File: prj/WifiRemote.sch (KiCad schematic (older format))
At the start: 68 parts, among them J1 DIP-BLACK-MALE-HEADER-VERT_4P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, J2 DIP-BLACK-MALE-HEADER_6P-2.54_, K1 DIP-SWITCH-TACTILE-SPST-NO_TS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, K2 DIP-SWITCH-TACTILE-SPST-NO_TS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, K3 DIP-SWITCH-TACTILE-SPST-NO_TS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, K4 DIP-SWITCH-TACTILE-SPST-NO_TS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, M1 Mechanical_Mount, M2 Mechanical_Mount, M3 Mechanical_Mount, M4 Mechanical_Mount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

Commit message: Changed button GPIO association and updated mechanical mount pin
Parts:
- M1, M2, M3, M4: footprint ICEE-Mechanical:mounting_panhead6_5mm -> (none)
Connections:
- net GPIO12: now also C9.2, D14.1, R30.1; no longer C6.2, D10.1, R27.1
- net GPIO13: now also D11.A (+), D7.A (+), D8.A (+), D9.A (+), R26.2; no longer C8.2, D13.1, R29.1
- net GPIO14: now also C8.2, D13.1, R29.1; no longer C9.2, D14.1, R30.1
- net GPIO4: now also C6.2, D10.1, R27.1; no longer D11.A (+), D7.A (+), D8.A (+), D9.A (+), R26.2
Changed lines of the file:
@@
 Text GLabel 6700 1400 2    39   Input ~ 0
 ESP_ADC
-Text GLabel 5675 3975 2    39   Input ~ 0
+Text GLabel 1325 3975 0    39   Input ~ 0
 GPIO4
 Text GLabel 2075 4225 0    39   Input ~ 0
 GPIO5
-Text GLabel 1325 3975 0    39   Input ~ 0
+Text GLabel 3750 4725 0    39   Input ~ 0
 GPIO12
+Text GLabel 5675 3975 2    39   Input ~ 0
+GPIO13
 Text GLabel 2950 4475 0    39   Input ~ 0
-GPIO13
-Text GLabel 3750 4725 0    39   Input ~ 0
 GPIO14
 $Comp
@@
 	4675 3975 1775 3975
 $Comp
-L Mechanical_Mount M1
-U 1 1 59BB9484
-P 7250 5800
-F 0 "M1" H 7150 5875 45  0000 L BNN
-F 1 "Mechanical_Mount" H 7050 5600 45  0001 L BNN
-F 2 "ICEE-Mechanical:mounting_panhead6_5mm" H 7250 5800 60  0001 C CNN
-F 3 "" H 7250 5800 60  0001 C CNN
-	1    7250 5800
-	1    0    0    -1
-$EndComp
-$Comp
-L Mechanical_Mount M2
-U 1 1 59BB9AA5
-P 7475 5800
-F 0 "M2" H 7375 5875 45  0000 L BNN
-F 1 "Mechanical_Mount" H 7275 5600 45  0001 L BNN
-F 2 "ICEE-Mechanical:mounting_panhead6_5mm" H 7475 5800 60  0001 C CNN
-F 3 "" H 7475 5800 60  0001 C CNN
-	1    7475 5800
-	1    0    0    -1
-$EndComp
-$Comp
-L Mechanical_Mount M3
-U 1 1 59BB9B95
-P 7700 5800
-F 0 "M3" H 7600 5875 45  0000 L BNN
-F 1 "Mechanical_Mount" H 7500 5600 45  0001 L BNN
-F 2 "ICEE-Mechanical:mounting_panhead6_5mm" H 7700 5800 60  0001 C CNN
-F 3 "" H 7700 5800 60  0001 C CNN
-	1    7700 5800
-	1    0    0    -1
-$EndComp
-$Comp
 L GNDD #PWR037
 U 1 1 59BC0554
@@
 F 3 "" H 7925 5900 50  0000 C CNN
 	1    7925 5900
-	1    0    0    -1
-$EndComp
-$Comp
-L Mechanical_Mount M4
-U 1 1 59BBA5DF
-P 7925 5800
-F 0 "M4" H 7825 5875 45  0000 L BNN
-F 1 "Mechanical_Mount" H 7725 5600 45  0001 L BNN
-F 2 "ICEE-Mechanical:mounting_panhead6_5mm" H 7925 5800 60  0001 C CNN
-F 3 "" H 7925 5800 60  0001 C CNN
-	1    7925 5800
 	1    0    0    -1
 $EndComp
@@
 	0    1    1    0
 $EndComp
+$Comp
+L Mechanical_Mount M1
+U 1 1 59C34B45
+P 7250 5800
+F 0 "M1" H 7150 5875 45  0000 L BNN
+F 1 "Mechanical_Mount" H 7300 5700 45  0001 L BNN
+F 2 "" H 7250 5800 60  0001 C CNN
+F 3 "" H 7250 5800 60  0001 C CNN
+	1    7250 5800
+	1    0    0    -1
+$EndComp
+$Comp
+L Mechanical_Mount M2
+U 1 1 59C35BEC
+P 7475 5800
+F 0 "M2" H 7375 5875 45  0000 L BNN
+F 1 "Mechanical_Mount" H 7525 5700 45  0001 L BNN
+F 2 "" H 7475 5800 60  0001 C CNN
+F 3 "" H 7475 5800 60  0001 C CNN
+	1    7475 5800
+	1    0    0    -1
+$EndComp
+$Comp
+L Mechanical_Mount M3
+U 1 1 59C35CD4
+P 7700 5800
+F 0 "M3" H 7600 5875 45  0000 L BNN
+F 1 "Mechanical_Mount" H 7750 5700 45  0001 L BNN
+F 2 "" H 7700 5800 60  0001 C CNN
+F 3 "" H 7700 5800 60  0001 C CNN
+	1    7700 5800
+	1    0    0    -1
+$EndComp
+$Comp
+L Mechanical_Mount M4
+U 1 1 59C35DC5
+P 7925 5800
+F 0 "M4" H 7825 5875 45  0000 L BNN
+F 1 "Mechanical_Mount" H 7975 5700 45  0001 L BNN
+F 2 "" H 7925 5800 60  0001 C CNN
+F 3 "" H 7925 5800 60  0001 C CNN
+	1    7925 5800
+	1    0    0    -1
+$EndComp
 $EndSCHEMATC

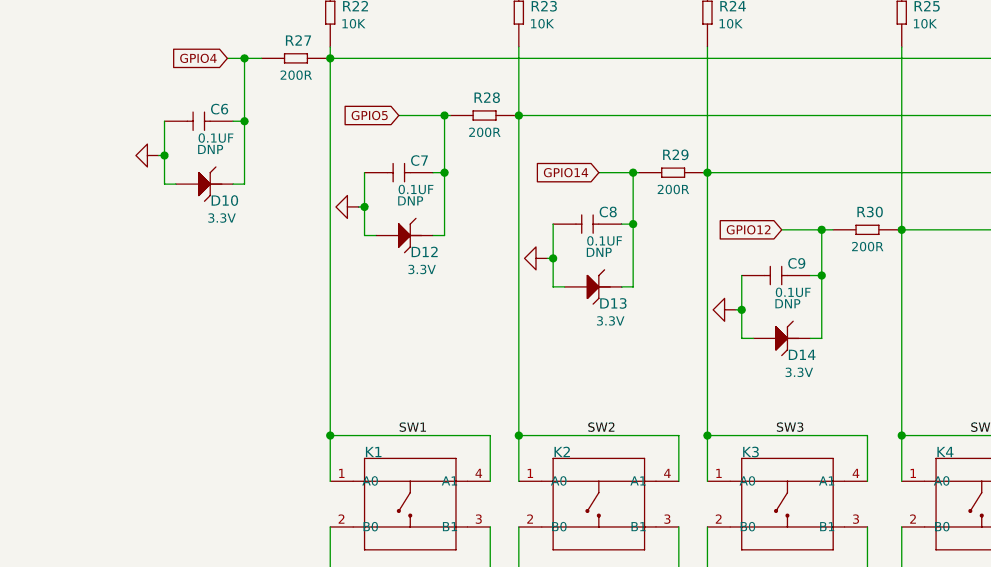
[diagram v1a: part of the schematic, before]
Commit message: Updated TVS diode pinout
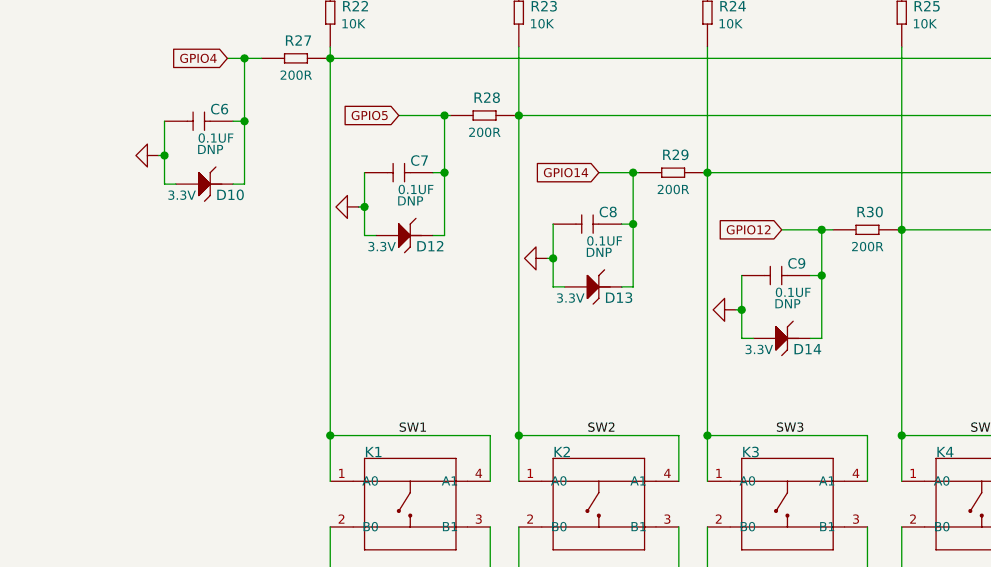
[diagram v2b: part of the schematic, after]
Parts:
- D10, D12, D13, D14, D4: footprint Diodes_SMD:SOD-523 -> Diodes_SMD:D_SOD-523
- M1, M2, M3, M4: footprint (none) -> ICEE-Mechanical:mounting_panhead6_5mm
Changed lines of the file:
@@
 NoConn ~ 250  -550
-$Comp
-L SMD-Diode-TVS-3.3VMW-15V-SOD-523 D14
-U 1 1 59B6E445
-P 3775 5200
-F 0 "D14" H 3775 5100 45  0000 L BNN
-F 1 "SMD-Diode-TVS-3.3VMW-15V-SOD-523" H 3625 5050 45  0001 L BNN
-F 2 "Diodes_SMD:SOD-523" H 3775 5200 60  0001 C CNN
-F 3 "" H 3775 5200 60  0000 C CNN
-F 4 "CJ;CESD3V3D5" H 3805 5350 20  0001 C CNN "MPN"
-F 5 "304060054" H 3805 5350 20  0001 C CNN "SKU"
-F 6 "SEEED" H 3775 5000 60  0001 C CNN "SUPPLIER"
-F 7 "3.3V" H 3825 5050 40  0000 C CNN "VBR"
-	1    3775 5200
-	1    0    0    -1
-$EndComp
 $Comp
 L DIP-BLACK-MALE-HEADER-VERT_4P-2.54_ J1
@@
 $EndComp
 $Comp
-L SMD-Diode-TVS-3.3VMW-15V-SOD-523 D4
-U 1 1 59B96847
-P 1425 2350
-F 0 "D4" V 1475 2250 45  0000 L BNN
-F 1 "SMD-Diode-TVS-3.3VMW-15V-SOD-523" H 1275 2200 45  0001 L BNN
-F 2 "Diodes_SMD:SOD-523" H 1425 2350 60  0001 C CNN
-F 3 "" H 1425 2350 60  0000 C CNN
-F 4 "CJ;CESD3V3D5" H 1455 2500 20  0001 C CNN "MPN"
-F 5 "304060054" H 1455 2500 20  0001 C CNN "SKU"
-F 6 "SEEED" H 1425 2150 60  0001 C CNN "SUPPLIER"
-F 7 "3.3V" V 1325 2275 40  0000 C CNN "VBR"
-	1    1425 2350
-	0    -1   -1   0
-$EndComp
-$Comp
 L GNDD #PWR031
 U 1 1 59B979E2
@@
 Connection ~ 4275 4725
 $Comp
-L SMD-Diode-TVS-3.3VMW-15V-SOD-523 D13
-U 1 1 59BFCBDB
-P 2950 4975
-F 0 "D13" H 2950 4875 45  0000 L BNN
-F 1 "SMD-Diode-TVS-3.3VMW-15V-SOD-523" H 2800 4825 45  0001 L BNN
-F 2 "Diodes_SMD:SOD-523" H 2950 4975 60  0001 C CNN
-F 3 "" H 2950 4975 60  0000 C CNN
-F 4 "CJ;CESD3V3D5" H 2980 5125 20  0001 C CNN "MPN"
-F 5 "304060054" H 2980 5125 20  0001 C CNN "SKU"
-F 6 "SEEED" H 2950 4775 60  0001 C CNN "SUPPLIER"
-F 7 "3.3V" H 3000 4825 40  0000 C CNN "VBR"
-	1    2950 4975
-	1    0    0    -1
-$EndComp
-$Comp
 L CERAMIC-100NF-50V-10%-X7R_0603_ C8
 U 1 1 59BFCBE4
@@
 Connection ~ 3100 4475
 $Comp
-L SMD-Diode-TVS-3.3VMW-15V-SOD-523 D12
-U 1 1 59BFE94D
-P 2125 4750
-F 0 "D12" H 2125 4650 45  0000 L BNN
-F 1 "SMD-Diode-TVS-3.3VMW-15V-SOD-523" H 1975 4600 45  0001 L BNN
-F 2 "Diodes_SMD:SOD-523" H 2125 4750 60  0001 C CNN
-F 3 "" H 2125 4750 60  0000 C CNN
-F 4 "CJ;CESD3V3D5" H 2155 4900 20  0001 C CNN "MPN"
-F 5 "304060054" H 2155 4900 20  0001 C CNN "SKU"
-F 6 "SEEED" H 2125 4550 60  0001 C CNN "SUPPLIER"
-F 7 "3.3V" H 2175 4600 40  0000 C CNN "VBR"
-	1    2125 4750
-	1    0    0    -1
-$EndComp
-$Comp
 L CERAMIC-100NF-50V-10%-X7R_0603_ C7
 U 1 1 59BFE956
@@
 Connection ~ 2600 4225
 $Comp
-L SMD-Diode-TVS-3.3VMW-15V-SOD-523 D10
-U 1 1 59C02DDD
-P 1250 4525
-F 0 "D10" H 1250 4425 45  0000 L BNN
-F 1 "SMD-Diode-TVS-3.3VMW-15V-SOD-523" H 1100 4375 45  0001 L BNN
-F 2 "Diodes_SMD:SOD-523" H 1250 4525 60  0001 C CNN
-F 3 "" H 1250 4525 60  0000 C CNN
-F 4 "CJ;CESD3V3D5" H 1280 4675 20  0001 C CNN "MPN"
-F 5 "304060054" H 1280 4675 20  0001 C CNN "SKU"
-F 6 "SEEED" H 1250 4325 60  0001 C CNN "SUPPLIER"
-F 7 "3.3V" H 1300 4375 40  0000 C CNN "VBR"
-	1    1250 4525
-	1    0    0    -1
-$EndComp
-$Comp
 L CERAMIC-100NF-50V-10%-X7R_0603_ C6
 U 1 1 59C02DE6
@@
 F 0 "M1" H 7150 5875 45  0000 L BNN
 F 1 "Mechanical_Mount" H 7300 5700 45  0001 L BNN
-F 2 "" H 7250 5800 60  0001 C CNN
+F 2 "ICEE-Mechanical:mounting_panhead6_5mm" H 7250 5800 60  0001 C CNN
 F 3 "" H 7250 5800 60  0001 C CNN
 	1    7250 5800
@@
 F 0 "M2" H 7375 5875 45  0000 L BNN
 F 1 "Mechanical_Mount" H 7525 5700 45  0001 L BNN
-F 2 "" H 7475 5800 60  0001 C CNN
+F 2 "ICEE-Mechanical:mounting_panhead6_5mm" H 7475 5800 60  0001 C CNN
 F 3 "" H 7475 5800 60  0001 C CNN
 	1    7475 5800
@@
 F 0 "M3" H 7600 5875 45  0000 L BNN
 F 1 "Mechanical_Mount" H 7750 5700 45  0001 L BNN
-F 2 "" H 7700 5800 60  0001 C CNN
+F 2 "ICEE-Mechanical:mounting_panhead6_5mm" H 7700 5800 60  0001 C CNN
 F 3 "" H 7700 5800 60  0001 C CNN
 	1    7700 5800
@@
 F 0 "M4" H 7825 5875 45  0000 L BNN
 F 1 "Mechanical_Mount" H 7975 5700 45  0001 L BNN
-F 2 "" H 7925 5800 60  0001 C CNN
+F 2 "ICEE-Mechanical:mounting_panhead6_5mm" H 7925 5800 60  0001 C CNN
 F 3 "" H 7925 5800 60  0001 C CNN
 	1    7925 5800
 	1    0    0    -1
 $EndComp
+$Comp
+L SMD-Diode-TVS-3.3VMW-15V-SOD-523 D4
+U 1 1 59C34CB4
+P 1425 2350
+F 0 "D4" V 1475 2250 45  0000 L BNN
+F 1 "SMD-Diode-TVS-3.3VMW-15V-SOD-523" H 1275 2200 45  0001 L BNN
+F 2 "Diodes_SMD:D_SOD-523" H 1425 2350 60  0001 C CNN
+F 3 "" H 1425 2350 60  0000 C CNN
+F 4 "CJ;CESD3V3D5" H 1455 2500 20  0001 C CNN "MPN"
+F 5 "304060054" H 1455 2500 20  0001 C CNN "SKU"
+F 6 "SEEED" H 1425 2150 60  0001 C CNN "SUPPLIER"
+F 7 "3.3V" V 1325 2275 40  0000 C CNN "VBR"
+	1    1425 2350
+	0    -1   -1   0
+$EndComp
+$Comp
+L SMD-Diode-TVS-3.3VMW-15V-SOD-523 D10
+U 1 1 59C35F11
+P 1250 4525
+F 0 "D10" H 1275 4450 45  0000 L BNN
+F 1 "SMD-Diode-TVS-3.3VMW-15V-SOD-523" H 1100 4375 45  0001 L BNN
+F 2 "Diodes_SMD:D_SOD-523" H 1250 4525 60  0001 C CNN
+F 3 "" H 1250 4525 60  0000 C CNN
+F 4 "CJ;CESD3V3D5" H 1280 4675 20  0001 C CNN "MPN"
+F 5 "304060054" H 1280 4675 20  0001 C CNN "SKU"
+F 6 "SEEED" H 1250 4325 60  0001 C CNN "SUPPLIER"
+F 7 "3.3V" H 1125 4475 40  0000 C CNN "VBR"
+	1    1250 4525
+	1    0    0    -1
+$EndComp
+$Comp
+L SMD-Diode-TVS-3.3VMW-15V-SOD-523 D12
+U 1 1 59C36ECC
+P 2125 4750
+F 0 "D12" H 2150 4675 45  0000 L BNN
+F 1 "SMD-Diode-TVS-3.3VMW-15V-SOD-523" H 1975 4600 45  0001 L BNN
+F 2 "Diodes_SMD:D_SOD-523" H 2125 4750 60  0001 C CNN
+F 3 "" H 2125 4750 60  0000 C CNN
+F 4 "CJ;CESD3V3D5" H 2155 4900 20  0001 C CNN "MPN"
+F 5 "304060054" H 2155 4900 20  0001 C CNN "SKU"
+F 6 "SEEED" H 2125 4550 60  0001 C CNN "SUPPLIER"
+F 7 "3.3V" H 2000 4700 40  0000 C CNN "VBR"
+	1    2125 4750
+	1    0    0    -1
+$EndComp
+$Comp
+L SMD-Diode-TVS-3.3VMW-15V-SOD-523 D13
+U 1 1 59C37B89
+P 2950 4975
+F 0 "D13" H 2975 4900 45  0000 L BNN
+F 1 "SMD-Diode-TVS-3.3VMW-15V-SOD-523" H 2800 4825 45  0001 L BNN
+F 2 "Diodes_SMD:D_SOD-523" H 2950 4975 60  0001 C CNN
+F 3 "" H 2950 4975 60  0000 C CNN
+F 4 "CJ;CESD3V3D5" H 2980 5125 20  0001 C CNN "MPN"
+F 5 "304060054" H 2980 5125 20  0001 C CNN "SKU"
+F 6 "SEEED" H 2950 4775 60  0001 C CNN "SUPPLIER"
+F 7 "3.3V" H 2825 4925 40  0000 C CNN "VBR"
+	1    2950 4975
+	1    0    0    -1
+$EndComp
+$Comp
+L SMD-Diode-TVS-3.3VMW-15V-SOD-523 D14
+U 1 1 59C38035
+P 3775 5200
+F 0 "D14" H 3800 5125 45  0000 L BNN
+F 1 "SMD-Diode-TVS-3.3VMW-15V-SOD-523" H 3625 5050 45  0001 L BNN
+F 2 "Diodes_SMD:D_SOD-523" H 3775 5200 60  0001 C CNN
+F 3 "" H 3775 5200 60  0000 C CNN
+F 4 "CJ;CESD3V3D5" H 3805 5350 20  0001 C CNN "MPN"
+F 5 "304060054" H 3805 5350 20  0001 C CNN "SKU"
+F 6 "SEEED" H 3775 5000 60  0001 C CNN "SUPPLIER"
+F 7 "3.3V" H 3650 5150 40  0000 C CNN "VBR"
+	1    3775 5200
+	1    0    0    -1
+$EndComp

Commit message: Added new SOD-523 diode footprint to ICEE library
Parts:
- D10, D12, D13, D14, D4: footprint Diodes_SMD:D_SOD-523 -> ICEE-Diode:SOD-523
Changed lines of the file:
@@
 F 0 "D4" V 1475 2250 45  0000 L BNN
 F 1 "SMD-Diode-TVS-3.3VMW-15V-SOD-523" H 1275 2200 45  0001 L BNN
-F 2 "Diodes_SMD:D_SOD-523" H 1425 2350 60  0001 C CNN
+F 2 "ICEE-Diode:SOD-523" H 1425 2350 60  0001 C CNN
 F 3 "" H 1425 2350 60  0000 C CNN
 F 4 "CJ;CESD3V3D5" H 1455 2500 20  0001 C CNN "MPN"
@@
 F 0 "D10" H 1275 4450 45  0000 L BNN
 F 1 "SMD-Diode-TVS-3.3VMW-15V-SOD-523" H 1100 4375 45  0001 L BNN
-F 2 "Diodes_SMD:D_SOD-523" H 1250 4525 60  0001 C CNN
+F 2 "ICEE-Diode:SOD-523" H 1250 4525 60  0001 C CNN
 F 3 "" H 1250 4525 60  0000 C CNN
 F 4 "CJ;CESD3V3D5" H 1280 4675 20  0001 C CNN "MPN"
@@
 F 0 "D12" H 2150 4675 45  0000 L BNN
 F 1 "SMD-Diode-TVS-3.3VMW-15V-SOD-523" H 1975 4600 45  0001 L BNN
-F 2 "Diodes_SMD:D_SOD-523" H 2125 4750 60  0001 C CNN
+F 2 "ICEE-Diode:SOD-523" H 2125 4750 60  0001 C CNN
 F 3 "" H 2125 4750 60  0000 C CNN
 F 4 "CJ;CESD3V3D5" H 2155 4900 20  0001 C CNN "MPN"
@@
 F 0 "D13" H 2975 4900 45  0000 L BNN
 F 1 "SMD-Diode-TVS-3.3VMW-15V-SOD-523" H 2800 4825 45  0001 L BNN
-F 2 "Diodes_SMD:D_SOD-523" H 2950 4975 60  0001 C CNN
+F 2 "ICEE-Diode:SOD-523" H 2950 4975 60  0001 C CNN
 F 3 "" H 2950 4975 60  0000 C CNN
 F 4 "CJ;CESD3V3D5" H 2980 5125 20  0001 C CNN "MPN"
@@
 F 0 "D14" H 3800 5125 45  0000 L BNN
 F 1 "SMD-Diode-TVS-3.3VMW-15V-SOD-523" H 3625 5050 45  0001 L BNN
-F 2 "Diodes_SMD:D_SOD-523" H 3775 5200 60  0001 C CNN
+F 2 "ICEE-Diode:SOD-523" H 3775 5200 60  0001 C CNN
 F 3 "" H 3775 5200 60  0000 C CNN
 F 4 "CJ;CESD3V3D5" H 3805 5350 20  0001 C CNN "MPN"

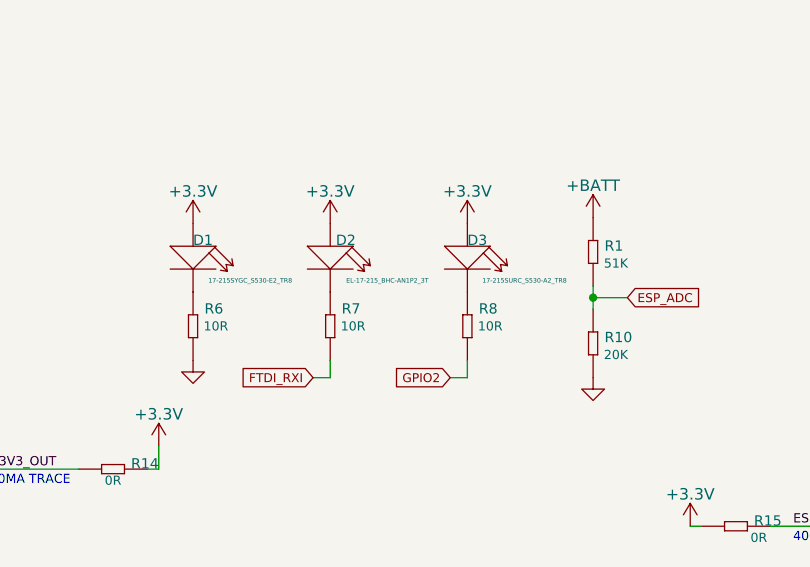
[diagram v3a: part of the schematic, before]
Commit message: Swapped D2 and D3
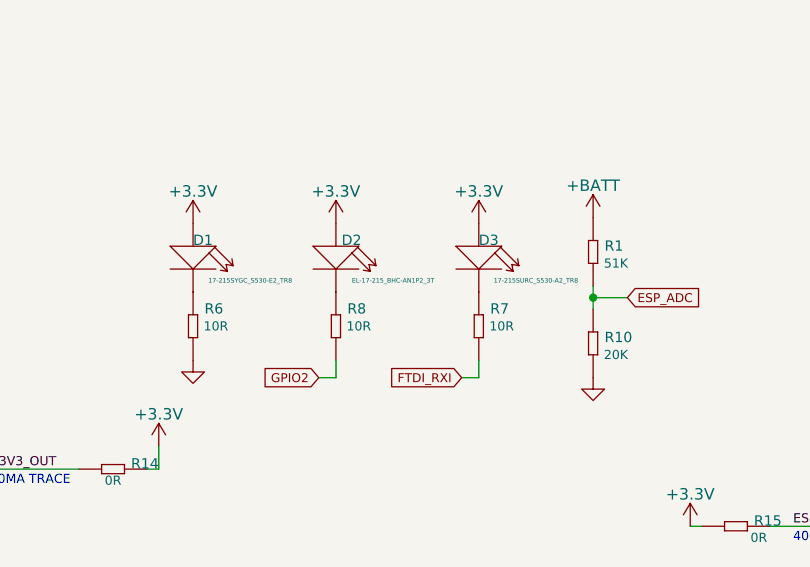
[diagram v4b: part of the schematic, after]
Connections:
- net at R7.1: now also D3.-; no longer D2.-
- net at R8.1: now also D2.-; no longer D3.-
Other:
- moved on the sheet: D2, D3, R7, R8
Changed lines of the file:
@@
 L SMD-RES-10R-5%-1_10W_0603_ R7
 U 1 1 59B36BCA
-P 5400 1525
-F 0 "R7" V 5350 1575 45  0000 L BNN
-F 1 "SMD-RES-10R-5%-1_10W_0603_" H 5250 1425 45  0001 L BNN
-F 2 "SeeedOPL-Resistor-2016:R0603" H 5400 1525 40  0001 C CNN
-F 3 "" H 5400 1525 40  0001 C CNN
-F 4 "RC0603JR-0710RL" H 5430 1675 20  0001 C CNN "MPN"
-F 5 "301010096" H 5430 1675 20  0001 C CNN "SKU"
-F 6 "10R" V 5400 1625 40  0000 C CNN "RESISTANCE"
-	1    5400 1525
+P 6050 1525
+F 0 "R7" V 6000 1575 45  0000 L BNN
+F 1 "SMD-RES-10R-5%-1_10W_0603_" H 5900 1425 45  0001 L BNN
+F 2 "SeeedOPL-Resistor-2016:R0603" H 6050 1525 40  0001 C CNN
+F 3 "" H 6050 1525 40  0001 C CNN
+F 4 "RC0603JR-0710RL" H 6080 1675 20  0001 C CNN "MPN"
+F 5 "301010096" H 6080 1675 20  0001 C CNN "SKU"
+F 6 "10R" V 6050 1625 40  0000 C CNN "RESISTANCE"
+	1    6050 1525
 	0    1    1    0
 $EndComp
@@
 	0    -1   -1   0
 $EndComp
-Text GLabel 5925 1750 0    39   Input ~ 0
+Text GLabel 5350 1750 0    39   Input ~ 0
 GPIO2
 Text GLabel 8000 1250 0    39   Input ~ 0
@@
 L +3.3V #PWR029
 U 1 1 59BA2283
-P 5400 1075
-F 0 "#PWR029" H 5400 925 50  0001 C CNN
-F 1 "+3.3V" H 5400 1215 50  0000 C CNN
-F 2 "" H 5400 1075 50  0000 C CNN
-F 3 "" H 5400 1075 50  0000 C CNN
-	1    5400 1075
+P 6050 1075
+F 0 "#PWR029" H 6050 925 50  0001 C CNN
+F 1 "+3.3V" H 6050 1215 50  0000 C CNN
+F 2 "" H 6050 1075 50  0000 C CNN
+F 3 "" H 6050 1075 50  0000 C CNN
+	1    6050 1075
 	1    0    0    -1
 $EndComp
@@
 L SMD-LED-CLEAR-RED_0805_ D3
 U 1 1 59B8C210
-P 6000 1225
-F 0 "D3" V 5950 1225 45  0000 L BNN
-F 1 "SMD-LED-CLEAR-RED_0805_" H 5800 1025 45  0001 L BNN
-F 2 "SeeedOPL-LED-2016:LED-0805" H 6000 1225 60  0001 C CNN
-F 3 "" H 6000 1225 60  0001 C CNN
-F 4 "17-215SURC_S530-A2_TR8" V 6100 1475 20  0000 C CNN "MPN"
-F 5 "304090046" H 6030 1375 20  0001 C CNN "SKU"
-	1    6000 1225
+P 6050 1225
+F 0 "D3" V 6000 1225 45  0000 L BNN
+F 1 "SMD-LED-CLEAR-RED_0805_" H 5850 1025 45  0001 L BNN
+F 2 "SeeedOPL-LED-2016:LED-0805" H 6050 1225 60  0001 C CNN
+F 3 "" H 6050 1225 60  0001 C CNN
+F 4 "17-215SURC_S530-A2_TR8" V 6150 1475 20  0000 C CNN "MPN"
+F 5 "304090046" H 6080 1375 20  0001 C CNN "SKU"
+	1    6050 1225
 	0    1    1    0
 $EndComp
@@
 L SMD-RES-10R-5%-1_10W_0603_ R8
 U 1 1 59B9052C
-P 6000 1525
-F 0 "R8" V 5950 1575 45  0000 L BNN
-F 1 "SMD-RES-10R-5%-1_10W_0603_" H 5850 1425 45  0001 L BNN
-F 2 "SeeedOPL-Resistor-2016:R0603" H 6000 1525 40  0001 C CNN
-F 3 "" H 6000 1525 40  0001 C CNN
-F 4 "RC0603JR-0710RL" H 6030 1675 20  0001 C CNN "MPN"
-F 5 "301010096" H 6030 1675 20  0001 C CNN "SKU"
-F 6 "10R" V 6000 1625 40  0000 C CNN "RESISTANCE"
-	1    6000 1525
-	0    1    1    0
-$EndComp
-Text GLabel 5325 1750 0    39   Input ~ 0
+P 5425 1525
+F 0 "R8" V 5375 1575 45  0000 L BNN
+F 1 "SMD-RES-10R-5%-1_10W_0603_" H 5275 1425 45  0001 L BNN
+F 2 "SeeedOPL-Resistor-2016:R0603" H 5425 1525 40  0001 C CNN
+F 3 "" H 5425 1525 40  0001 C CNN
+F 4 "RC0603JR-0710RL" H 5455 1675 20  0001 C CNN "MPN"
+F 5 "301010096" H 5455 1675 20  0001 C CNN "SKU"
+F 6 "10R" V 5425 1625 40  0000 C CNN "RESISTANCE"
+	1    5425 1525
+	0    1    1    0
+$EndComp
+Text GLabel 5975 1750 0    39   Input ~ 0
 FTDI_RXI
 $Comp
 L +3.3V #PWR030
 U 1 1 59B94182
-P 6000 1075
-F 0 "#PWR030" H 6000 925 50  0001 C CNN
-F 1 "+3.3V" H 6000 1215 50  0000 C CNN
-F 2 "" H 6000 1075 50  0000 C CNN
-F 3 "" H 6000 1075 50  0000 C CNN
-	1    6000 1075
+P 5425 1075
+F 0 "#PWR030" H 5425 925 50  0001 C CNN
+F 1 "+3.3V" H 5425 1215 50  0000 C CNN
+F 2 "" H 5425 1075 50  0000 C CNN
+F 3 "" H 5425 1075 50  0000 C CNN
+	1    5425 1075
 	1    0    0    -1
 $EndComp
@@
 	7850 2425 7850 2400
 Wire Wire Line
-	5925 1750 6000 1750
-Wire Wire Line
-	6000 1750 6000 1675
-Wire Wire Line
-	5325 1750 5400 1750
-Wire Wire Line
-	5400 1750 5400 1675
+	5350 1750 5425 1750
+Wire Wire Line
+	5425 1750 5425 1675
+Wire Wire Line
+	5975 1750 6050 1750
+Wire Wire Line
+	6050 1750 6050 1675
 Wire Wire Line
 	1425 2250 1425 2150
@@
 L SMD-LED-CLEAR-BLUE_0805_ D2
 U 1 1 59C1E2BF
-P 5400 1225
-F 0 "D2" V 5350 1250 45  0000 L BNN
-F 1 "SMD-LED-CLEAR-BLUE_0805_" H 5200 1025 45  0001 L BNN
-F 2 "SeeedOPL-LED-2016:LED-0805" H 5400 1225 60  0001 C CNN
-F 3 "" H 5400 1225 60  0001 C CNN
-F 4 "EL-17-215_BHC-AN1P2_3T" V 5500 1475 20  0000 C CNN "MPN"
-F 5 "304090061" H 5430 1375 20  0001 C CNN "SKU"
-	1    5400 1225
-	0    1    1    0
-$EndComp
+P 5425 1225
+F 0 "D2" V 5375 1250 45  0000 L BNN
+F 1 "SMD-LED-CLEAR-BLUE_0805_" H 5225 1025 45  0001 L BNN
+F 2 "SeeedOPL-LED-2016:LED-0805" H 5425 1225 60  0001 C CNN
+F 3 "" H 5425 1225 60  0001 C CNN
+F 4 "EL-17-215_BHC-AN1P2_3T" V 5525 1475 20  0000 C CNN "MPN"
+F 5 "304090061" H 5455 1375 20  0001 C CNN "SKU"
+	1    5425 1225
+	0    1    1    0
+$EndComp
